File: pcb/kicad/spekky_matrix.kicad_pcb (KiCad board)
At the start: 2 copper layers, 330 parts, among them J1 USB_B_Micro, J2 Conn_ARM_JTAG_SWD_10, Q1 DMP3125L-7, Q2 DMP3125L-7, Q3 DMP3125L-7, Q4 DMP3125L-7, Q5 DMP3125L-7, Q6 DMP3125L-7, Q7 DMP3125L-7, Q8 DMP3125L-7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

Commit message: Add pcb constraint settings (oshpark)
- Used OSHPark constraints and haven't had any issues with either
  Elecrow or OSHPark
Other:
- rule pad_to_mask_clearance: 0 -> 0.0508
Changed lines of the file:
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@@
 	)
 	(setup
-		(pad_to_mask_clearance 0)
+		(stackup
+			(layer "F.SilkS"
+				(type "Top Silk Screen")
+			)
+			(layer "F.Paste"
+				(type "Top Solder Paste")
+			)
+			(layer "F.Mask"
+				(type "Top Solder Mask")
+				(thickness 0.01)
+			)
+			(layer "F.Cu"
+				(type "copper")
+				(thickness 0.035)
+			)
+			(layer "dielectric 1"
+				(type "core")
+				(thickness 1.51)
+				(material "FR4")
+				(epsilon_r 4.5)
+				(loss_tangent 0.02)
+			)
+			(layer "B.Cu"
+				(type "copper")
+				(thickness 0.035)
+			)
+			(layer "B.Mask"
+				(type "Bottom Solder Mask")
+				(thickness 0.01)
+			)
+			(layer "B.Paste"
+				(type "Bottom Solder Paste")
+			)
+			(layer "B.SilkS"
+				(type "Bottom Silk Screen")
+			)
+			(copper_finish "None")
+			(dielectric_constraints no)
+		)
+		(pad_to_mask_clearance 0.0508)
 		(allow_soldermask_bridges_in_footprints no)
 		(tenting front back)

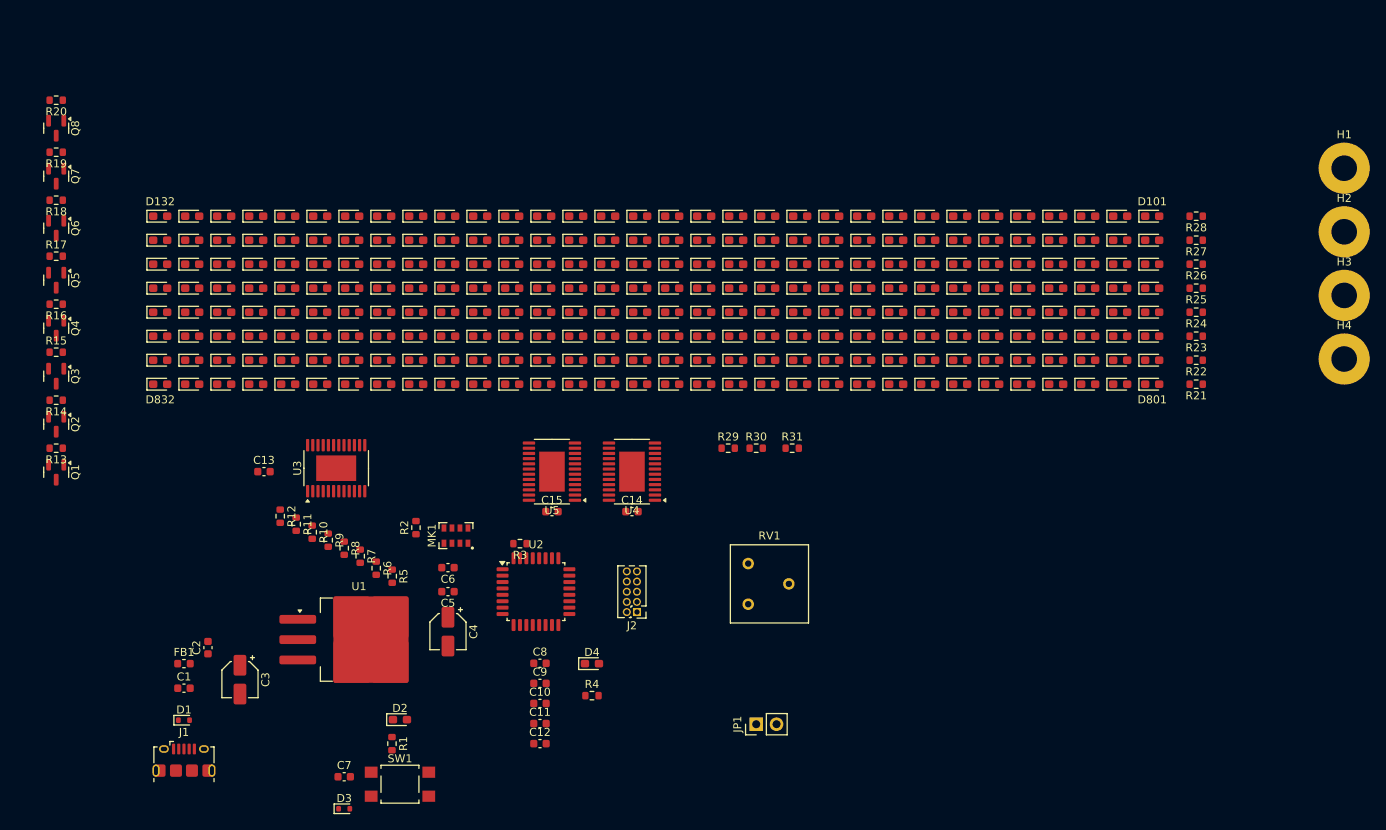
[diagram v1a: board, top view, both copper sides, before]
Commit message: Add pcb edge cuts with initial power traces (rough)
- Initial rough draft of PCB edge cuts (with curved corners) and power
  traces
- Added a "user.4" lines to show the PCB layout without curved edges
- Edge cuts are 153x96 mm
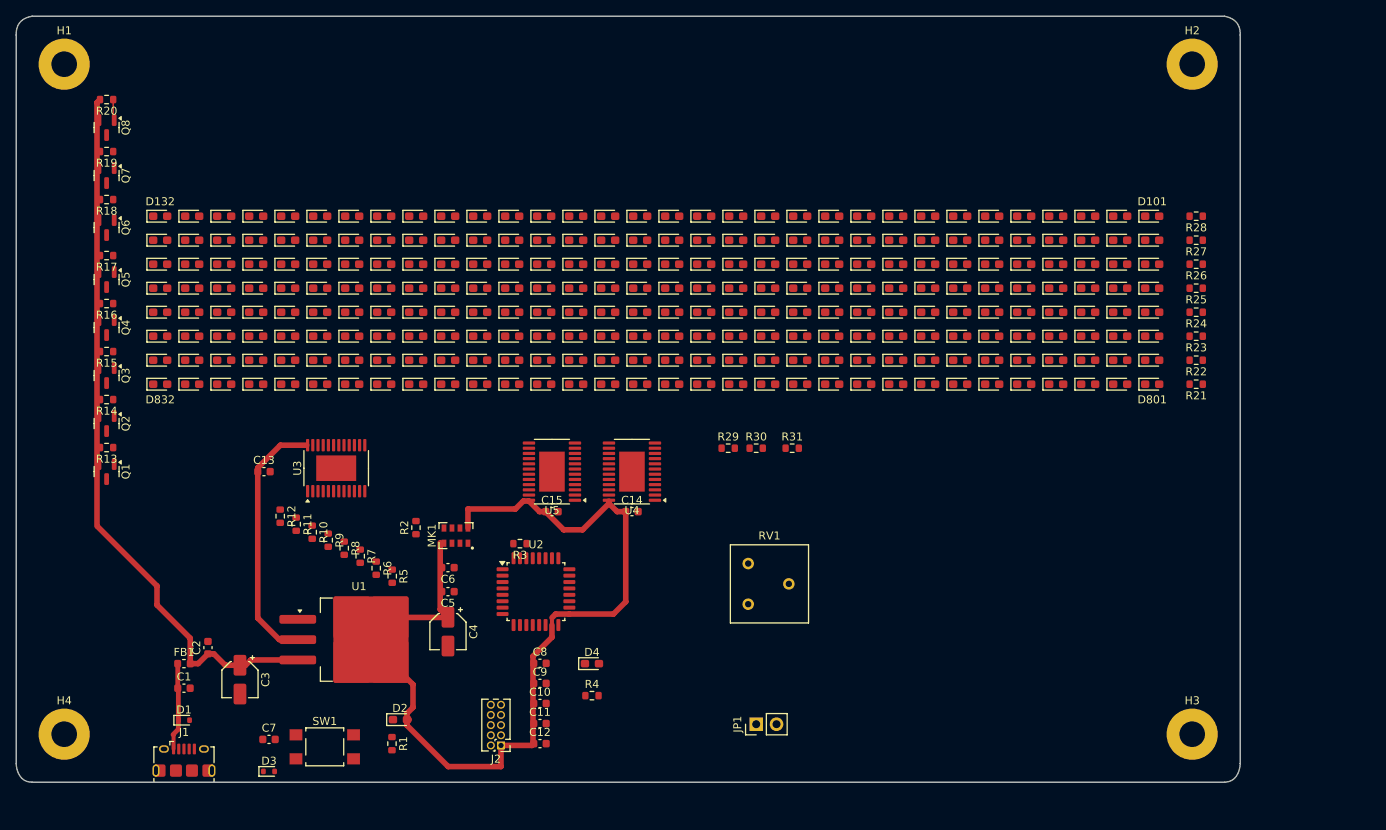
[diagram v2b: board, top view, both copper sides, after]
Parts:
- moved H4 166.7 mm to (61.0, 126.8)
- moved H1 160.5 mm to (61.0, 43.0)
- moved H3 58.0 mm to (202.0, 126.8)
- moved H2 28.3 mm to (202.0, 43.0)
- moved J2 23.8 mm to (115.6, 128.2)
- moved C7 10.5 mm to (86.6, 127.4)
- moved D3 10.5 mm to (86.6, 131.4)
- moved SW1 10.5 mm to (93.6, 128.3)
- moved Q1 6.30 mm to (66.3, 93.9)
- moved Q2 6.30 mm to (66.3, 87.9)
- moved Q3 6.30 mm to (66.3, 81.9)
- moved Q4 6.30 mm to (66.3, 75.9)
- moved Q5 6.30 mm to (66.3, 69.9)
- moved Q6 6.30 mm to (66.3, 63.4)
- moved Q7 6.30 mm to (66.3, 56.9)
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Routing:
- net +3V3: track 0.00 -> 143.1 mm
- net +5V: track 0.00 -> 90.2 mm
- net VBUS: track 0.00 -> 11.0 mm
- net Net-(Q8-G): track 0.00 -> 2.61 mm
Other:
- board outline added: 153 x 95.8 mm

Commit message: Connect up led row/col signal paths on pcb
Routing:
- net /LED DRIVING/ROW8: track 0.00 -> 146.2 mm, vias 0 -> 2
- net /LED DRIVING/ROW1: track 0.00 -> 143.4 mm, vias 0 -> 2
- net /LED DRIVING/ROW7: track 0.00 -> 142.9 mm, vias 0 -> 2
- net /LED DRIVING/ROW2: track 0.00 -> 142.0 mm, vias 0 -> 2
- net /LED DRIVING/ROW6: track 0.00 -> 140.6 mm, vias 0 -> 2
- net /LED DRIVING/ROW5: track 0.00 -> 138.2 mm, vias 0 -> 2
- net /LED DRIVING/ROW3: track 0.00 -> 137.5 mm, vias 0 -> 2
- net /LED DRIVING/ROW4: track 0.00 -> 135.4 mm, vias 0 -> 2
- net /LED DRIVING/COL9: track 0.00 -> 21.0 mm
- net /LED DRIVING/COL8: track 0.00 -> 21.0 mm
- net /LED DRIVING/COL7: track 0.00 -> 21.0 mm
- net /LED DRIVING/COL6: track 0.00 -> 21.0 mm
- net /LED DRIVING/COL5: track 0.00 -> 21.0 mm
- net /LED DRIVING/COL4: track 0.00 -> 21.0 mm
- net /LED DRIVING/COL32: track 0.00 -> 21.0 mm
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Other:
- board text removed: "ROWS on Bcu COLS on Fcu"

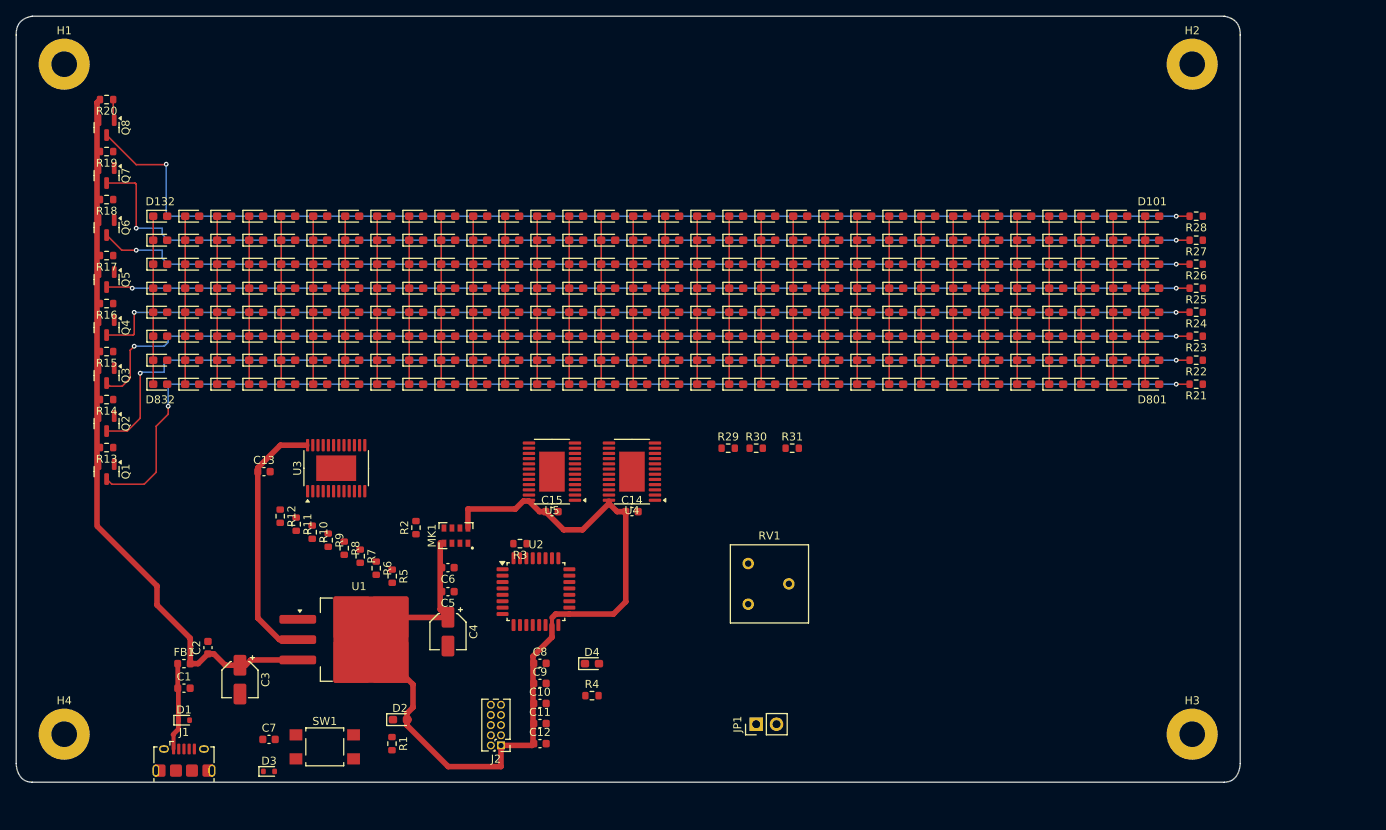
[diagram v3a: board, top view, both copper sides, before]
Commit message: Add gnd copper pours for entire front and back of pcb
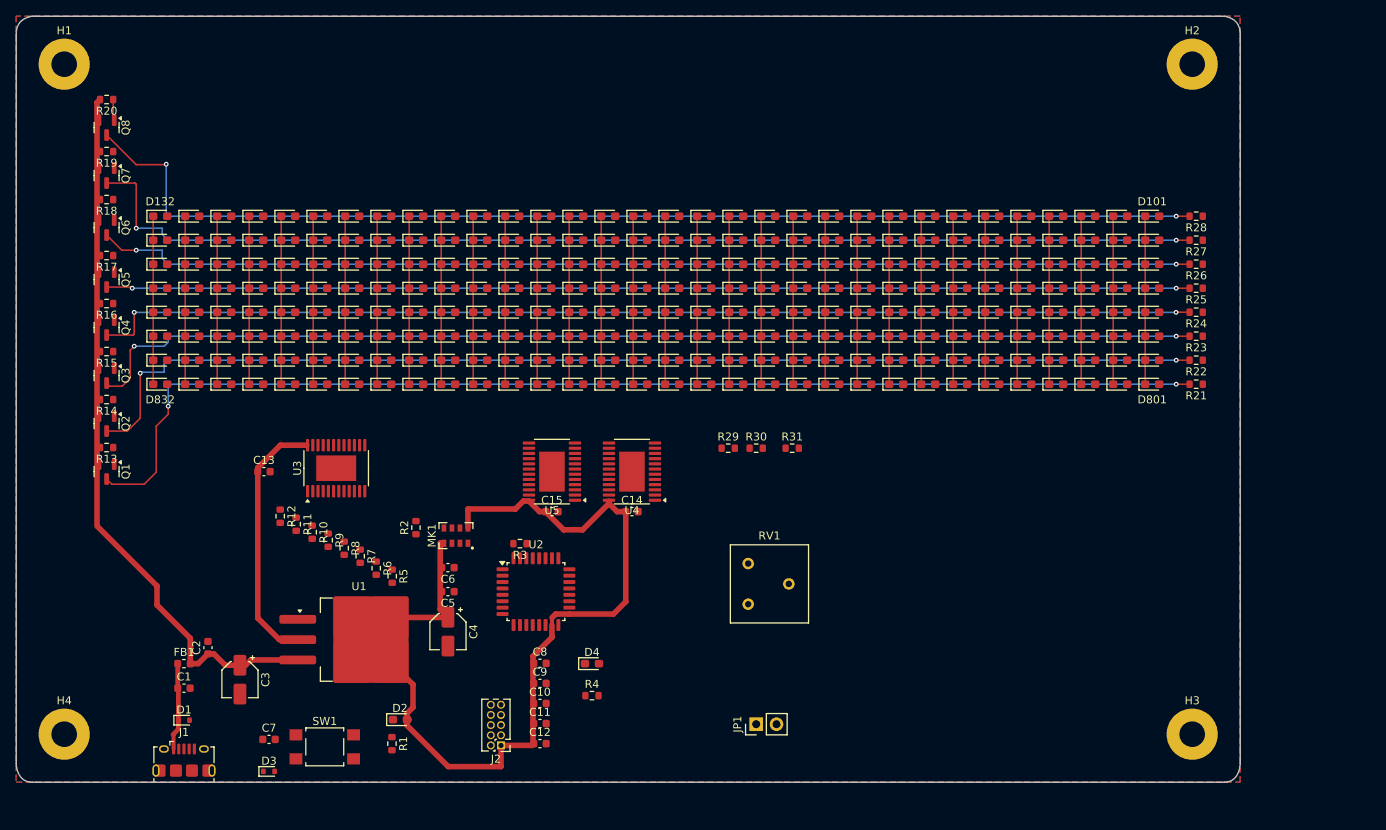
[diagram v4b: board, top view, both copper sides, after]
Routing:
- added copper zone on B.Cu, net GND
- added copper zone on F.Cu, net GND
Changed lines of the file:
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@@
 		(net 68)
+	)
+	(zone
+		(net 2)
+		(net_name "GND")
+		(layer "F.Cu")
+		(hatch edge 0.5)
+		(connect_pads
+			(clearance 0.5)
+		)
+		(min_thickness 0.25)
+		(filled_areas_thickness no)
+		(fill yes
+			(thermal_gap 0.5)
+			(thermal_bridge_width 0.5)
+		)
+		(polygon
+			(pts
+				(xy 55 37) (xy 55 132.75) (xy 208 132.75) (xy 208 37)
+			)
+		)
+	)
+	(zone
+		(net 2)
+		(net_name "GND")
+		(layer "B.Cu")
+		(hatch edge 0.5)
+		(priority 1)
+		(connect_pads
+			(clearance 0.5)
+		)
+		(min_thickness 0.25)
+		(filled_areas_thickness no)
+		(fill yes
+			(thermal_gap 0.5)
+			(thermal_bridge_width 0.5)
+		)
+		(polygon
+			(pts
+				(xy 55 37) (xy 55 132.75) (xy 208 132.75) (xy 208 37)
+			)
+		)
 	)
 	(embedded_fonts no)

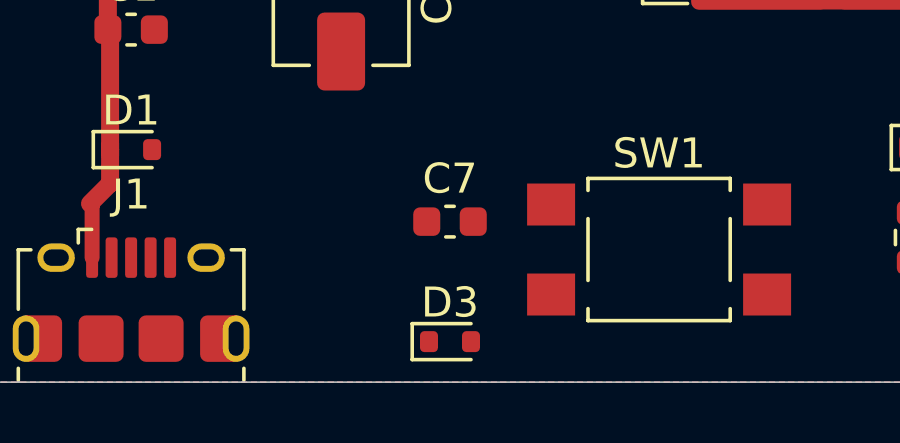
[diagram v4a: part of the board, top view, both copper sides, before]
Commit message: Move d3 on pcb (line up nrst signals vertically)
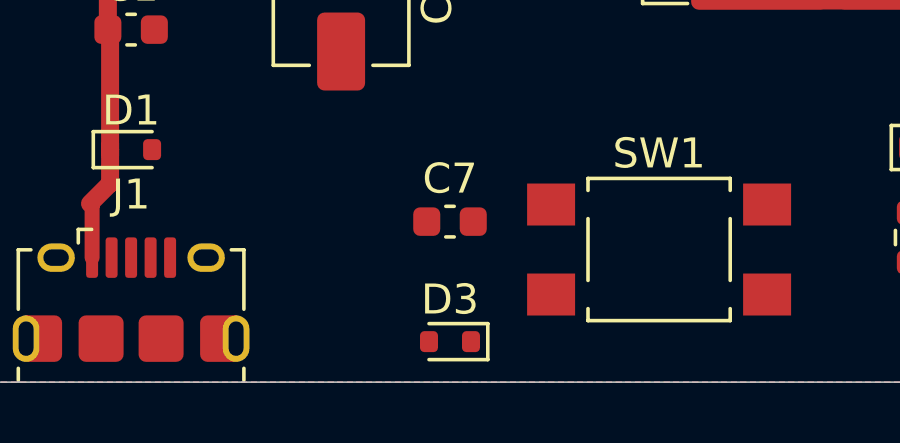
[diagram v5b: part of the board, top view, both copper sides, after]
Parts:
- turned D3 to 180 degrees
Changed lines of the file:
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@@
 	(footprint "Diode_SMD:D_SOD-523"
 		(layer "F.Cu")
-		(at 86.6 131.4)
+		(at 86.6 131.4 180)
 		(descr "http://www.diodes.com/datasheets/ap02001.pdf p.144")
 		(tags "Diode SOD523")
 		(property "Reference" "D3"
-			(at 0 -1.3 0)
+			(at 0 1.4 0)
 			(layer "F.SilkS")
 			(effects
@@
 		)
 		(property "Datasheet" ""
-			(at 0 0 0)
+			(at 0 0 180)
 			(unlocked yes)
 			(layer "F.Fab")
@@
 		)
 		(property "Description" "5V, TVS unidirectional diode"
-			(at 0 0 0)
+			(at 0 0 180)
 			(unlocked yes)
 			(layer "F.Fab")
@@
 		)
 		(property "MPN" "PESD5V0X1UAB,115"
-			(at 0 0 0)
+			(at 0 0 180)
 			(unlocked yes)
 			(layer "F.Fab")
@@
 		(attr smd)
 		(fp_line
+			(start 0.7 0.6)
+			(end -1.26 0.6)
+			(stroke
+				(width 0.12)
+				(type solid)
+			)
+			(layer "F.SilkS")
+		)
+		(fp_line
+			(start 0.7 -0.6)
+			(end -1.26 -0.6)
+			(stroke
+				(width 0.12)
+				(type solid)
+			)
+			(layer "F.SilkS")
+		)
+		(fp_line
 			(start -1.26 -0.6)
 			(end -1.26 0.6)
@@
 		)
 		(fp_line
-			(start 0.7 -0.6)
-			(end -1.26 -0.6)
-			(stroke
-				(width 0.12)
-				(type solid)
-			)
-			(layer "F.SilkS")
-		)
-		(fp_line
-			(start 0.7 0.6)
-			(end -1.26 0.6)
-			(stroke
-				(width 0.12)
-				(type solid)
-			)
-			(layer "F.SilkS")
+			(start 1.25 0.7)
+			(end -1.25 0.7)
+			(stroke
+				(width 0.05)
+				(type solid)
+			)
+			(layer "F.CrtYd")
+		)
+		(fp_line
+			(start 1.25 -0.7)
+			(end 1.25 0.7)
+			(stroke
+				(width 0.05)
+				(type solid)
+			)
+			(layer "F.CrtYd")
+		)
+		(fp_line
+			(start -1.25 0.7)
+			(end -1.25 -0.7)
+			(stroke
+				(width 0.05)
+				(type solid)
+			)
+			(layer "F.CrtYd")
 		)
 		(fp_line
@@
 		)
 		(fp_line
-			(start -1.25 0.7)
-			(end -1.25 -0.7)
-			(stroke
-				(width 0.05)
-				(type solid)
-			)
-			(layer "F.CrtYd")
-		)
-		(fp_line
-			(start 1.25 -0.7)
-			(end 1.25 0.7)
-			(stroke
-				(width 0.05)
-				(type solid)
-			)
-			(layer "F.CrtYd")
-		)
-		(fp_line
-			(start 1.25 0.7)
-			(end -1.25 0.7)
-			(stroke
-				(width 0.05)
-				(type solid)
-			)
-			(layer "F.CrtYd")
+			(start 0.65 0.45)
+			(end -0.65 0.45)
+			(stroke
+				(width 0.1)
+				(type solid)
+			)
+			(layer "F.Fab")
+		)
+		(fp_line
+			(start 0.65 -0.45)
+			(end 0.65 0.45)
+			(stroke
+				(width 0.1)
+				(type solid)
+			)
+			(layer "F.Fab")
+		)
+		(fp_line
+			(start 0.1 0.2)
+			(end 0.1 -0.2)
+			(stroke
+				(width 0.1)
+				(type solid)
+			)
+			(layer "F.Fab")
+		)
+		(fp_line
+			(start 0.1 0)
+			(end 0.25 0)
+			(stroke
+				(width 0.1)
+				(type solid)
+			)
+			(layer "F.Fab")
+		)
+		(fp_line
+			(start 0.1 -0.2)
+			(end -0.2 0)
+			(stroke
+				(width 0.1)
+				(type solid)
+			)
+			(layer "F.Fab")
+		)
+		(fp_line
+			(start -0.2 0.2)
+			(end -0.2 -0.2)
+			(stroke
+				(width 0.1)
+				(type solid)
+			)
+			(layer "F.Fab")
+		)
+		(fp_line
+			(start -0.2 0)
+			(end 0.1 0.2)
+			(stroke
+				(width 0.1)
+				(type solid)
+			)
+			(layer "F.Fab")
+		)
+		(fp_line
+			(start -0.2 0)
+			(end -0.35 0)
+			(stroke
+				(width 0.1)
+				(type solid)
+			)
+			(layer "F.Fab")
+		)
+		(fp_line
+			(start -0.65 0.45)
+			(end -0.65 -0.45)
+			(stroke
+				(width 0.1)
+				(type solid)
+			)
+			(layer "F.Fab")
 		)
 		(fp_line
@@
 			(layer "F.Fab")
 		)
-		(fp_line
-			(start -0.65 0.45)
-			(end -0.65 -0.45)
-			(stroke
-				(width 0.1)
-				(type solid)
-			)
-			(layer "F.Fab")
-		)
-		(fp_line
-			(start -0.2 0)
-			(end -0.35 0)
-			(stroke
-				(width 0.1)
-				(type solid)
-			)
-			(layer "F.Fab")
-		)
-		(fp_line
-			(start -0.2 0)
-			(end 0.1 0.2)
-			(stroke
-				(width 0.1)
-				(type solid)
-			)
-			(layer "F.Fab")
-		)
-		(fp_line
-			(start -0.2 0.2)
-			(end -0.2 -0.2)
-			(stroke
-				(width 0.1)
-				(type solid)
-			)
-			(layer "F.Fab")
-		)
-		(fp_line
-			(start 0.1 -0.2)
-			(end -0.2 0)
-			(stroke
-				(width 0.1)
-				(type solid)
-			)
-			(layer "F.Fab")
-		)
-		(fp_line
-			(start 0.1 0)
-			(end 0.25 0)
-			(stroke
-				(width 0.1)
-				(type solid)
-			)
-			(layer "F.Fab")
-		)
-		(fp_line
-			(start 0.1 0.2)
-			(end 0.1 -0.2)
-			(stroke
-				(width 0.1)
-				(type solid)
-			)
-			(layer "F.Fab")
-		)
-		(fp_line
-			(start 0.65 -0.45)
-			(end 0.65 0.45)
-			(stroke
-				(width 0.1)
-				(type solid)
-			)
-			(layer "F.Fab")
-		)
-		(fp_line
-			(start 0.65 0.45)
-			(end -0.65 0.45)
-			(stroke
-				(width 0.1)
-				(type solid)
-			)
-			(layer "F.Fab")
-		)
 		(fp_text user "${REFERENCE}"
-			(at 0 -1.3 0)
+			(at 0 1.4 0)
 			(layer "F.Fab")
 			(effects
@@
 		)
 		(pad "1" smd roundrect
-			(at -0.7 0 180)
+			(at -0.7 0)
 			(size 0.6 0.7)
 			(layers "F.Cu" "F.Mask" "F.Paste")
@@
 		)
 		(pad "2" smd roundrect
-			(at 0.7 0 180)
+			(at 0.7 0)
 			(size 0.6 0.7)
 			(layers "F.Cu" "F.Mask" "F.Paste")
